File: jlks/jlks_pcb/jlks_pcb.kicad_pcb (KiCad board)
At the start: 2 copper layers, 114.3 x 99.4 mm, 27 parts, among them J0 Conn_01x02_Socket, SW0 SW_Push, SW1 SW_Push, SW10 SW_Push, SW11 SW_Push, SW12 SW_Push, SW13 SW_Push, SW14 SW_Push, SW15 SW_Push, SW16 SW_Push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

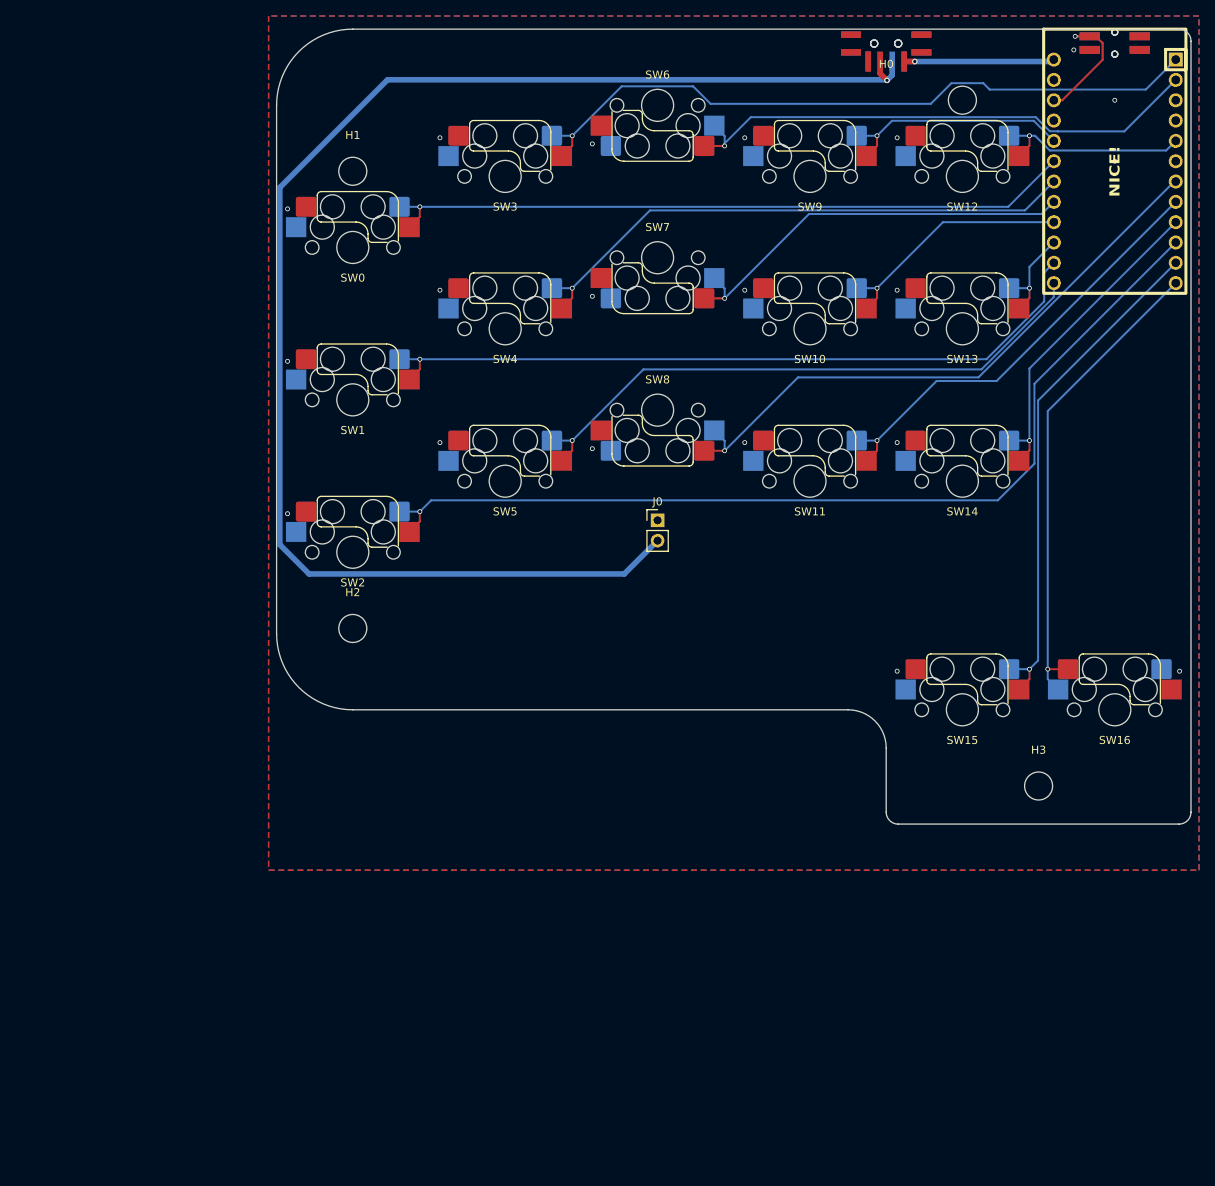
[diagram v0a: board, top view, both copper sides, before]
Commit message: Changed out the power switch and reset button on jlks.
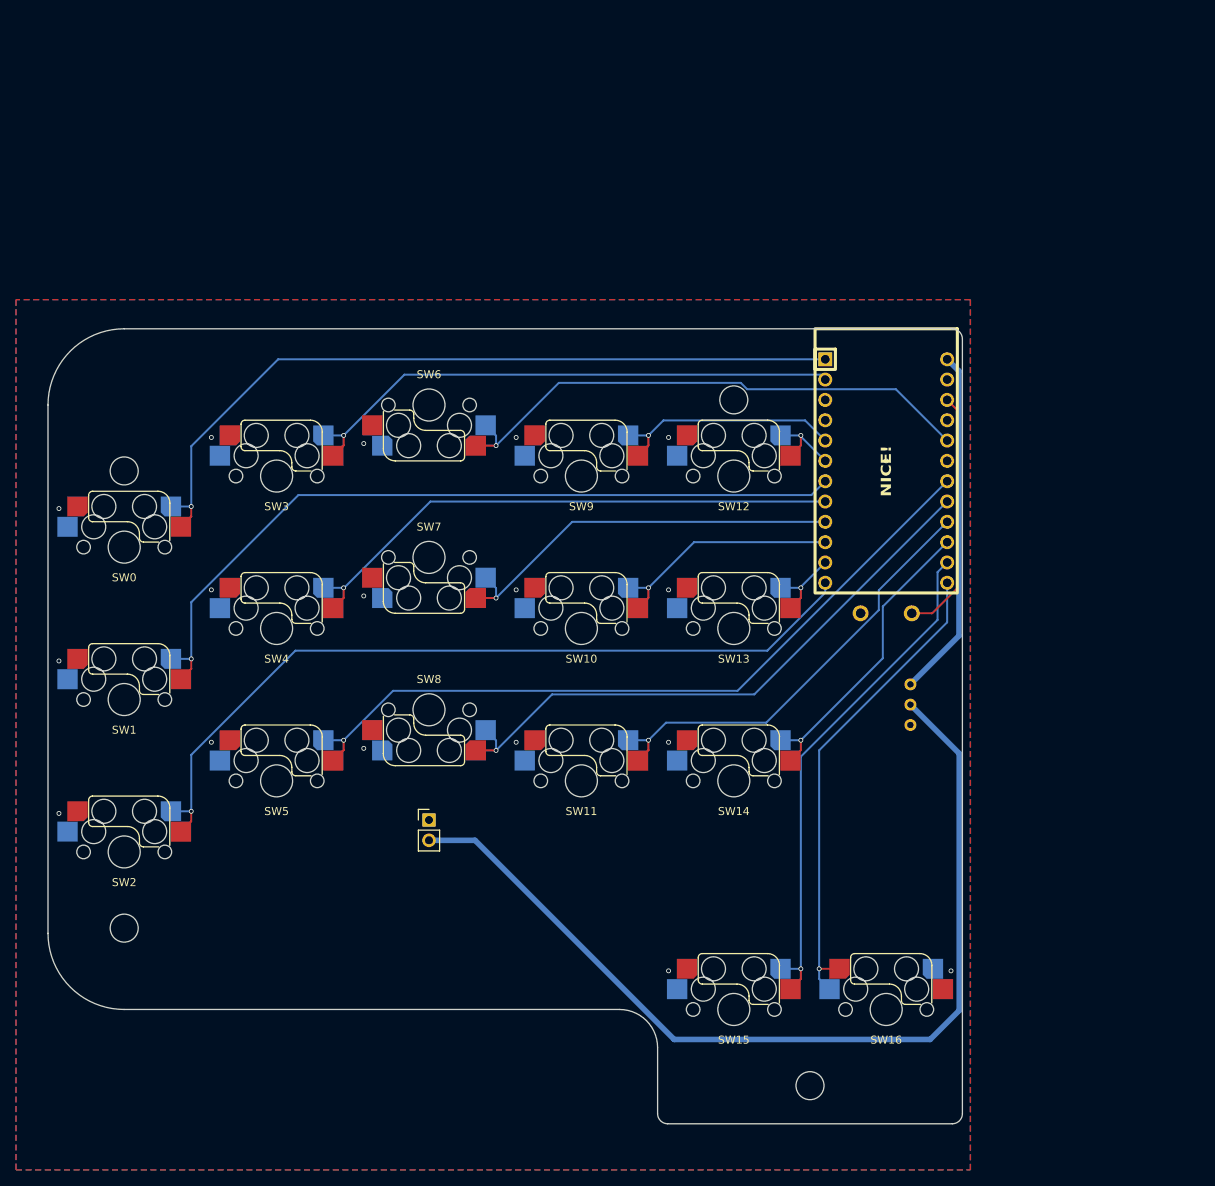
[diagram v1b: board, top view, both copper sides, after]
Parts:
- removed PWR1: POWER, footprints:power_switch
- removed RST1: RESET, footprints:reset_button_2
- PWR0: footprint footprints:power_switch -> footprints:power_switch_1
- RST0: footprint footprints:reset_button_2 -> footprints:reset_button; moved to B.Cu
- U0: moved to F.Cu
- moved PWR0 85.0 mm to (171.4, 95.2), turned to -90 degrees
- moved RST0 76.8 mm to (161.9, 83.8), turned to 0 degrees
- moved H1 47.1 mm to (66.7, 66.0)
- moved H2 47.1 mm to (66.7, 123.2)
- moved SW11 47.1 mm to (123.8, 104.8)
- moved SW2 47.1 mm to (66.7, 113.7)
- moved SW5 47.1 mm to (85.7, 104.8)
- moved H3 47.1 mm to (152.4, 142.9)
- moved SW0 47.1 mm to (66.7, 75.6)
- moved SW1 47.1 mm to (66.7, 94.6)
- moved SW10 47.1 mm to (123.8, 85.7)
- moved SW14 47.1 mm to (142.9, 104.8)
- moved SW3 47.1 mm to (85.7, 66.7)
- moved SW4 47.1 mm to (85.7, 85.7)
- moved SW6 47.1 mm to (104.8, 57.8)
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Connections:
- U0 pad 1: /KEY3 -> /KEY0
- U0 pad 10: /KEY2 -> /KEY10
- U0 pad 11: /KEY15 -> /KEY13
- U0 pad 12: /KEY16 -> /KEY2
- U0 pad 13: /KEY5 -> /KEY16
- U0 pad 14: /KEY1 -> /KEY15
- U0 pad 15: /KEY13 -> /KEY14
- U0 pad 16: /KEY10 -> /KEY11
- U0 pad 17: /KEY7 -> /KEY8
- U0 pad 18: /KEY4 -> /KEY5
- U0 pad 19: /KEY0 -> unconnected-(U0-F5-Pad19)
- U0 pad 2: /KEY6 -> /KEY3
- U0 pad 20: /KEY9 -> /KEY6
- U0 pad 5: /KEY12 -> /KEY9
- U0 pad 6: unconnected-(U0-SCL-Pad6) -> /KEY12
- U0 pad 7: /KEY8 -> /KEY1
- U0 pad 8: /KEY11 -> /KEY4
- U0 pad 9: /KEY14 -> /KEY7
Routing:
- net /B+: track 181.9 -> 118.8 mm, vias 1 -> 0
- net /RAW: track 20.1 -> 43.8 mm, vias 1 -> 0
- net /KEY5: track 75.0 -> 94.5 mm
- net /KEY2: track 119.9 -> 101.6 mm
- net /KEY3: track 87.5 -> 69.2 mm
- net /RST: track 14.1 -> 31.0 mm, vias 1 -> 0
- net /KEY12: track 25.2 -> 10.1 mm
- net /KEY0: track 87.2 -> 96.9 mm
- net /KEY1: track 92.0 -> 98.2 mm
- net /KEY14: track 40.5 -> 38.0 mm
- net /KEY13: track 12.6 -> 10.0 mm
- net /KEY6: track 66.8 -> 68.2 mm
- net /KEY10: track 31.1 -> 30.1 mm
- net /KEY8: track 75.9 -> 74.9 mm
- net /KEY7: track 51.8 -> 50.7 mm
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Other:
- outline, holes or cut-outs redrawn

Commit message: Updates to jlks, added corresponding top and bottom plates.
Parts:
- moved H2 14.6 mm to (78.2, 114.3)
- moved J0 7.73 mm to (112.5, 110.0)
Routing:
- net /B+: track 118.8 -> 111.0 mm
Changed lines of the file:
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@@
   (net 24 "unconnected-(U0-F5-Pad19)")
   (footprint "MountingHole:MountingHole_3.5mm" (layer "F.Cu")
-    (at 66.675 123.183161)
+    (at 78.2 114.3)
     (descr "Mounting Hole 3.5mm, no annular")
     (tags "mounting hole 3.5mm no annular")
@@
   )
   (footprint "Connector_PinHeader_2.54mm:PinHeader_1x02_P2.54mm_Vertical" (layer "F.Cu")
-    (at 104.775 109.666839)
+    (at 112.5 109.96)
     (descr "Through hole straight pin header, 1x02, 2.54mm pitch, single row")
     (tags "Through hole pin header THT 1x02 2.54mm single row")
@@
   (segment (start 169.545 57.156839) (end 170.7463 58.358139) (width 0.25) (layer "F.Cu") (net 20))
   (segment (start 170.7463 58.358139) (end 170.7463 80.7537) (width 0.25) (layer "F.Cu") (net 20))
-  (segment (start 135.425 137.1) (end 167.425 137.1) (width 0.7) (layer "B.Cu") (net 22))
   (segment (start 171.05 101.35) (end 164.95 95.25) (width 0.7) (layer "B.Cu") (net 22))
+  (segment (start 167.425 137.1) (end 137.1 137.1) (width 0.7) (layer "B.Cu") (net 22))
   (segment (start 167.425 137.1) (end 171.05 133.475) (width 0.7) (layer "B.Cu") (net 22))
-  (segment (start 110.531839 112.206839) (end 135.425 137.1) (width 0.7) (layer "B.Cu") (net 22))
+  (segment (start 137.1 137.1) (end 112.5 112.5) (width 0.7) (layer "B.Cu") (net 22))
   (segment (start 171.05 133.475) (end 171.05 101.35) (width 0.7) (layer "B.Cu") (net 22))
-  (segment (start 104.775 112.206839) (end 110.531839 112.206839) (width 0.7) (layer "B.Cu") (net 22))
   (zone (net 1) (net_name "GND") (layers "F&B.Cu") (hatch edge 0.5)
     (connect_pads (clearance 0.508))
